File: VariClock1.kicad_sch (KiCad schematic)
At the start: 71 parts, among them U32 40106, U33 4013, U34 40106, U35 40193, U36 TL074, U37 4042, U38 40193

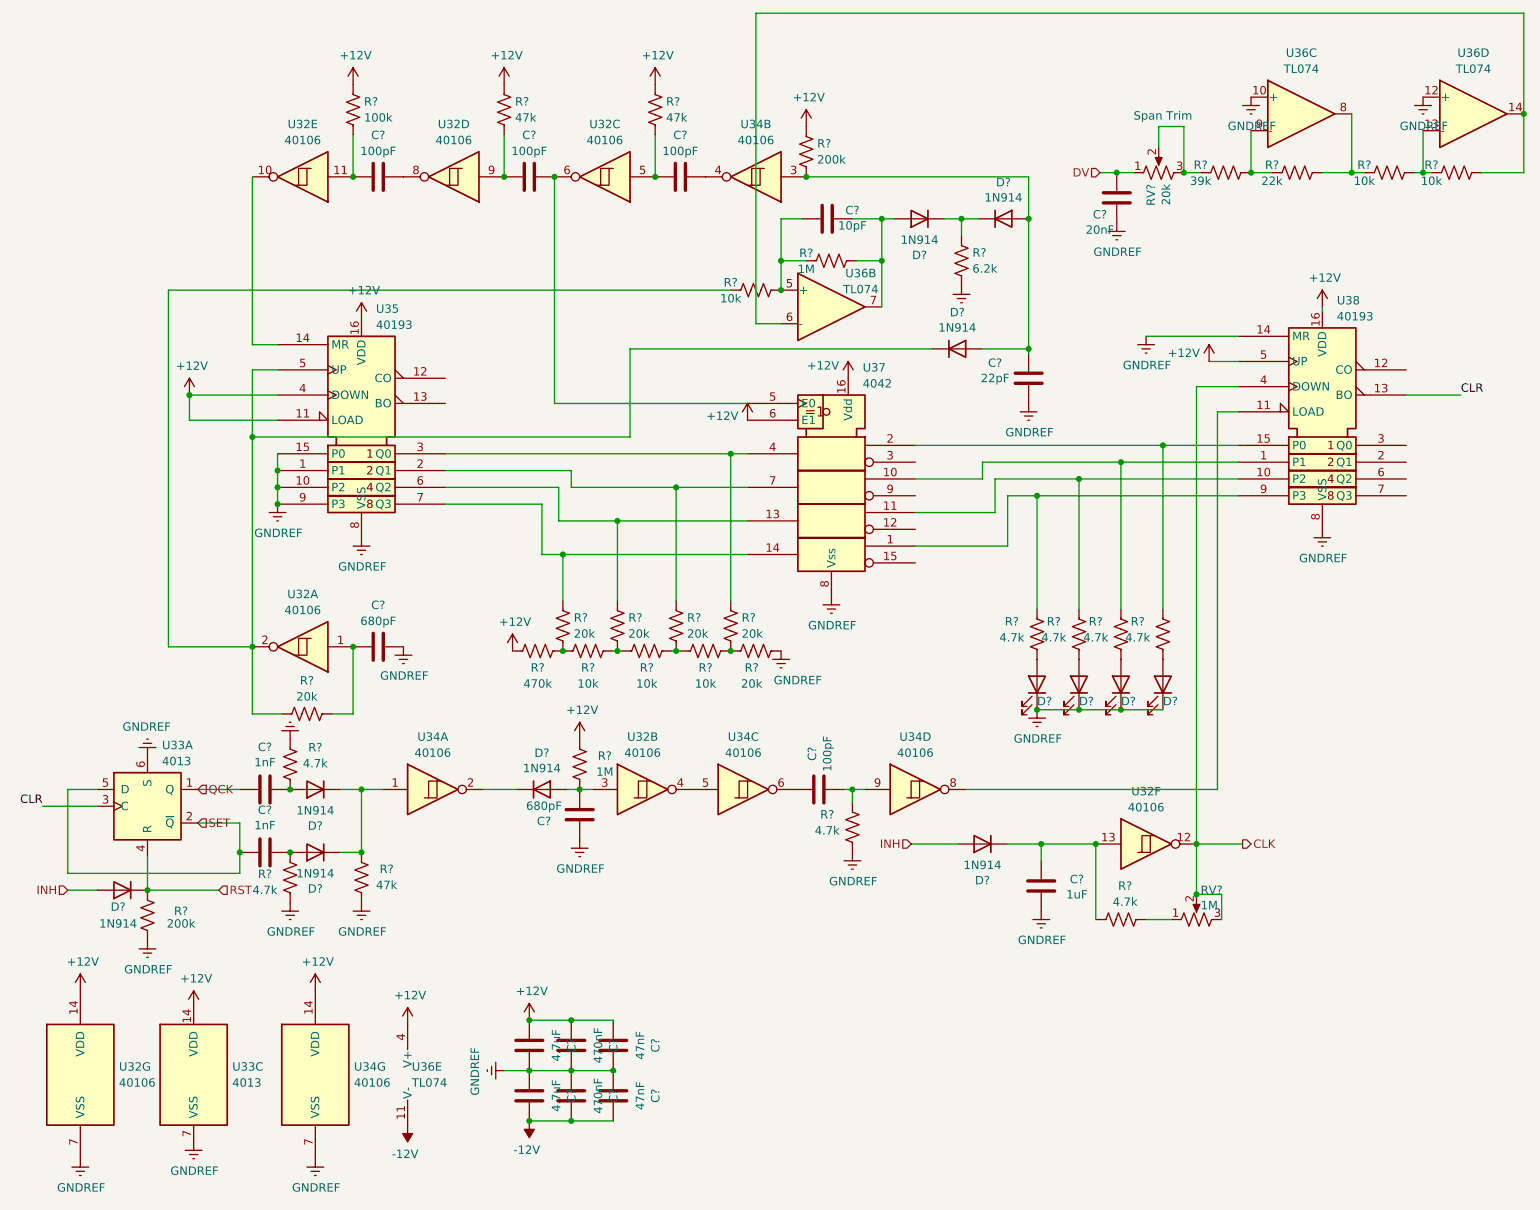
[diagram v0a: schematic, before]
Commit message: created pcb file, placed parts
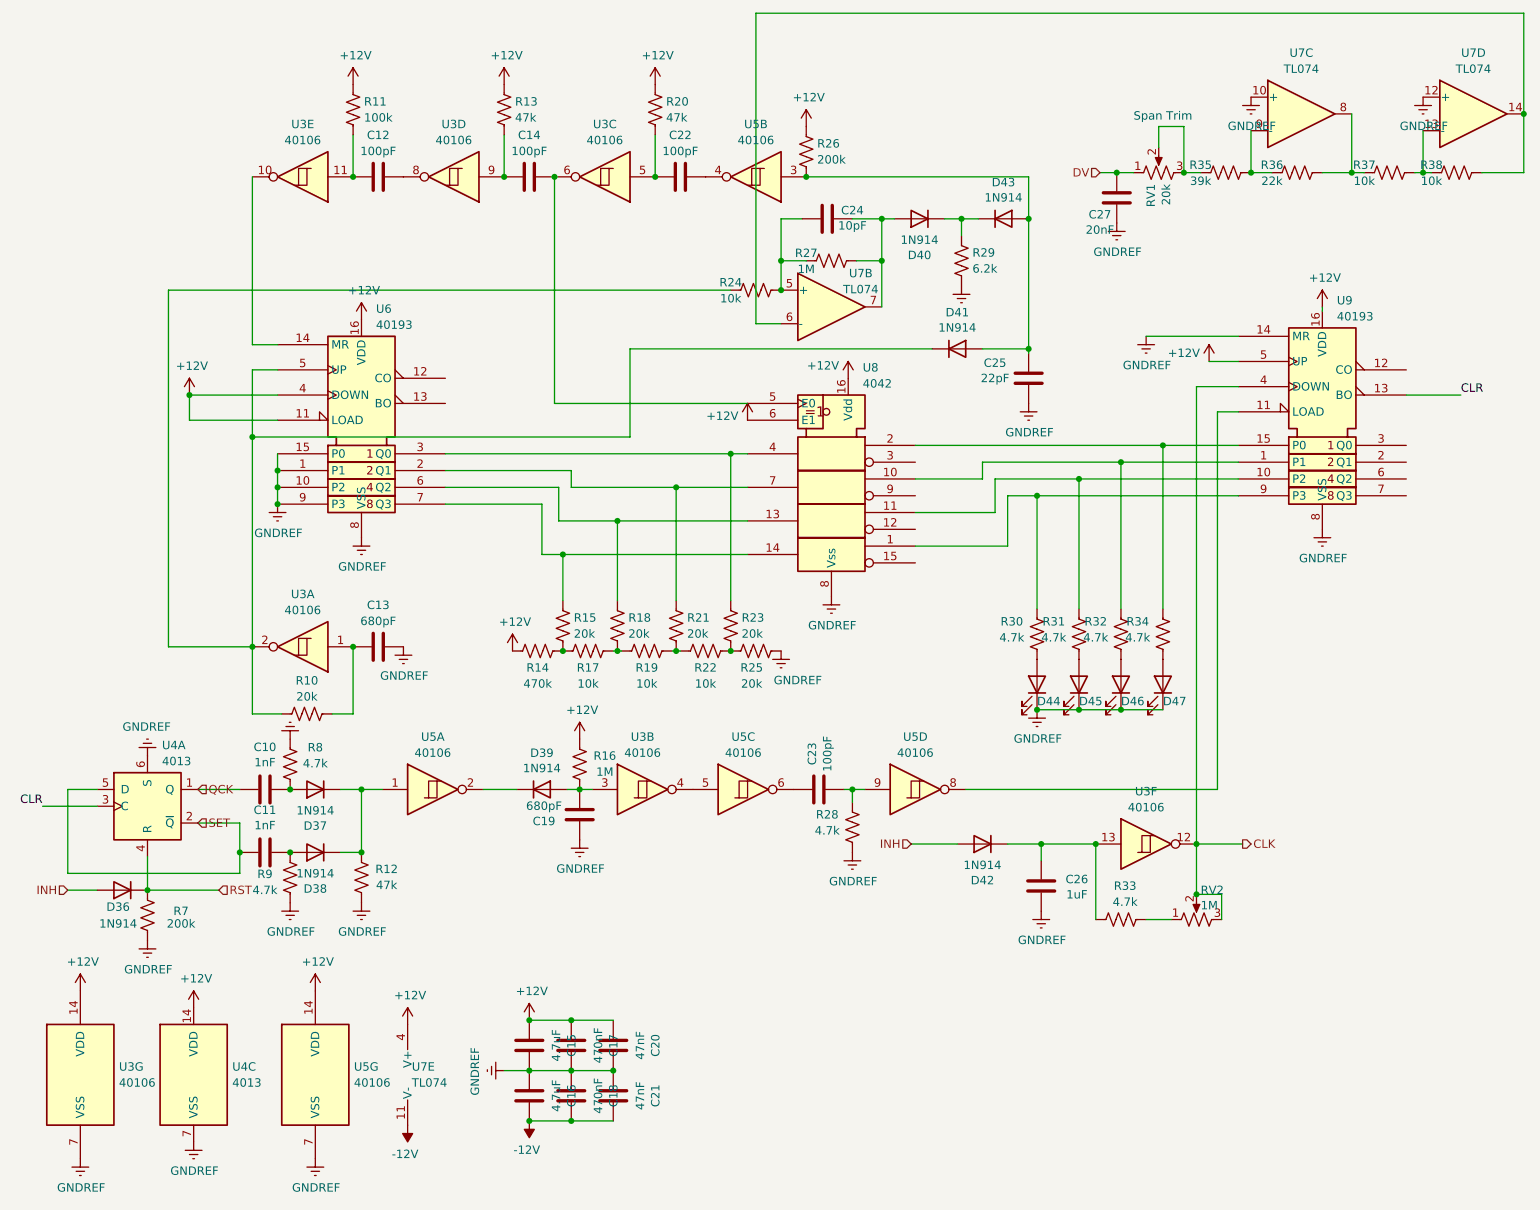
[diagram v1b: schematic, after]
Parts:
- gave numbers to parts that had none: 64
- renumbered U32 to U3, U33 to U4, U34 to U5, U35 to U6, U36 to U7, U37 to U8, U38 to U9

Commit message: init placement/layout
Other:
- note added: "Clock Rate"
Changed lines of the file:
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@@
+    (effects (font (size 1.27 1.27)) (justify left bottom))
+  )
+  (text "Clock Rate" (at 204.47 149.86 0)
     (effects (font (size 1.27 1.27)) (justify left bottom))
   )

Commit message: routing and placing
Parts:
- D44, D45, D46, D47: footprint LED_SMD:LED_0805_2012Metric -> LED_THT:LED_D5.0mm
- renumbered U5 to U3, U3 to U5
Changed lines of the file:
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@@
   (symbol (lib_id "4xxx:40106") (at 116.84 135.89 0) (unit 2)
     (in_bom yes) (on_board yes) (dnp no) (fields_autoplaced)
-    (property "Reference" "U3" (at 116.84 127.9357 0)
-      (effects (font (size 1.27 1.27)))
-    )
-    (property "Value" "40106" (at 116.84 130.3599 0)
+    (property "Reference" "U5" (at 116.84 127 0)
+      (effects (font (size 1.27 1.27)))
+    )
+    (property "Value" "40106" (at 116.84 129.54 0)
       (effects (font (size 1.27 1.27)))
     )
@@
       (project "SoundLab16StepSequencer"
         (path "/0a1377c9-61ff-44bc-b9df-99baf54c0c4b/a120791a-9c87-4325-b919-053c468d1b1e"
-          (reference "U3") (unit 2)
+          (reference "U5") (unit 2)
         )
       )
@@
       (effects (font (size 1.27 1.27)) (justify left) hide)
     )
-    (property "Footprint" "LED_SMD:LED_0805_2012Metric" (at 182.88 120.015 0)
+    (property "Footprint" "LED_THT:LED_D5.0mm" (at 182.88 120.015 0)
       (effects (font (size 1.27 1.27)) hide)
     )
@@
       (effects (font (size 1.27 1.27)) (justify left) hide)
     )
-    (property "Footprint" "LED_SMD:LED_0805_2012Metric" (at 195.58 120.015 0)
+    (property "Footprint" "LED_THT:LED_D5.0mm" (at 195.58 120.015 0)
       (effects (font (size 1.27 1.27)) hide)
     )
@@
   (symbol (lib_id "4xxx:40106") (at 133.985 43.18 180) (unit 2)
     (in_bom yes) (on_board yes) (dnp no)
-    (property "Reference" "U5" (at 133.985 35.2257 0)
+    (property "Reference" "U3" (at 133.985 35.2257 0)
       (effects (font (size 1.27 1.27)))
     )
@@
       (project "SoundLab16StepSequencer"
         (path "/0a1377c9-61ff-44bc-b9df-99baf54c0c4b/a120791a-9c87-4325-b919-053c468d1b1e"
-          (reference "U5") (unit 2)
+          (reference "U3") (unit 2)
         )
       )
@@
       (effects (font (size 1.27 1.27)) (justify left) hide)
     )
-    (property "Footprint" "LED_SMD:LED_0805_2012Metric" (at 189.23 120.015 0)
+    (property "Footprint" "LED_THT:LED_D5.0mm" (at 189.23 120.015 0)
       (effects (font (size 1.27 1.27)) hide)
     )
@@
       (effects (font (size 1.27 1.27)) (justify left) hide)
     )
-    (property "Footprint" "LED_SMD:LED_0805_2012Metric" (at 176.53 120.015 0)
-      (effects (font (size 1.27 1.27)) hide)
-    )
+    (property "Footprint" "LED_THT:LED_D5.0mm" (at 176.53 120.015 0)
+      (effects (font (size 1.27 1.27)) hide)
+    )

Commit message: routed 100%
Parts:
- removed C15, C16: 4.7uF, Capacitor_SMD:C_0805_2012Metric, symbol Device:C
- removed C17, C18: 470nF, Capacitor_SMD:C_0805_2012Metric, symbol Device:C
- removed C20, C21: 47nF, Capacitor_SMD:C_0603_1608Metric, symbol Device:C
- added C52 (x6): 470nF, Capacitor_SMD:C_0805_2012Metric, symbol Device:C
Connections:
- net +12V: now also C52.1, C52.1, C52.1, C52.1, C52.1, C52.1
- net GNDREF: now also C52.2, C52.2, C52.2, C52.2, C52.2, C52.2
